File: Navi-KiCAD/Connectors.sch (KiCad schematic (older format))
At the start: 7 parts, among them J4 473460001, J5 AXK5S80047YG, J6 AXK5S80047YG, U13 NUF2042XV6T1G

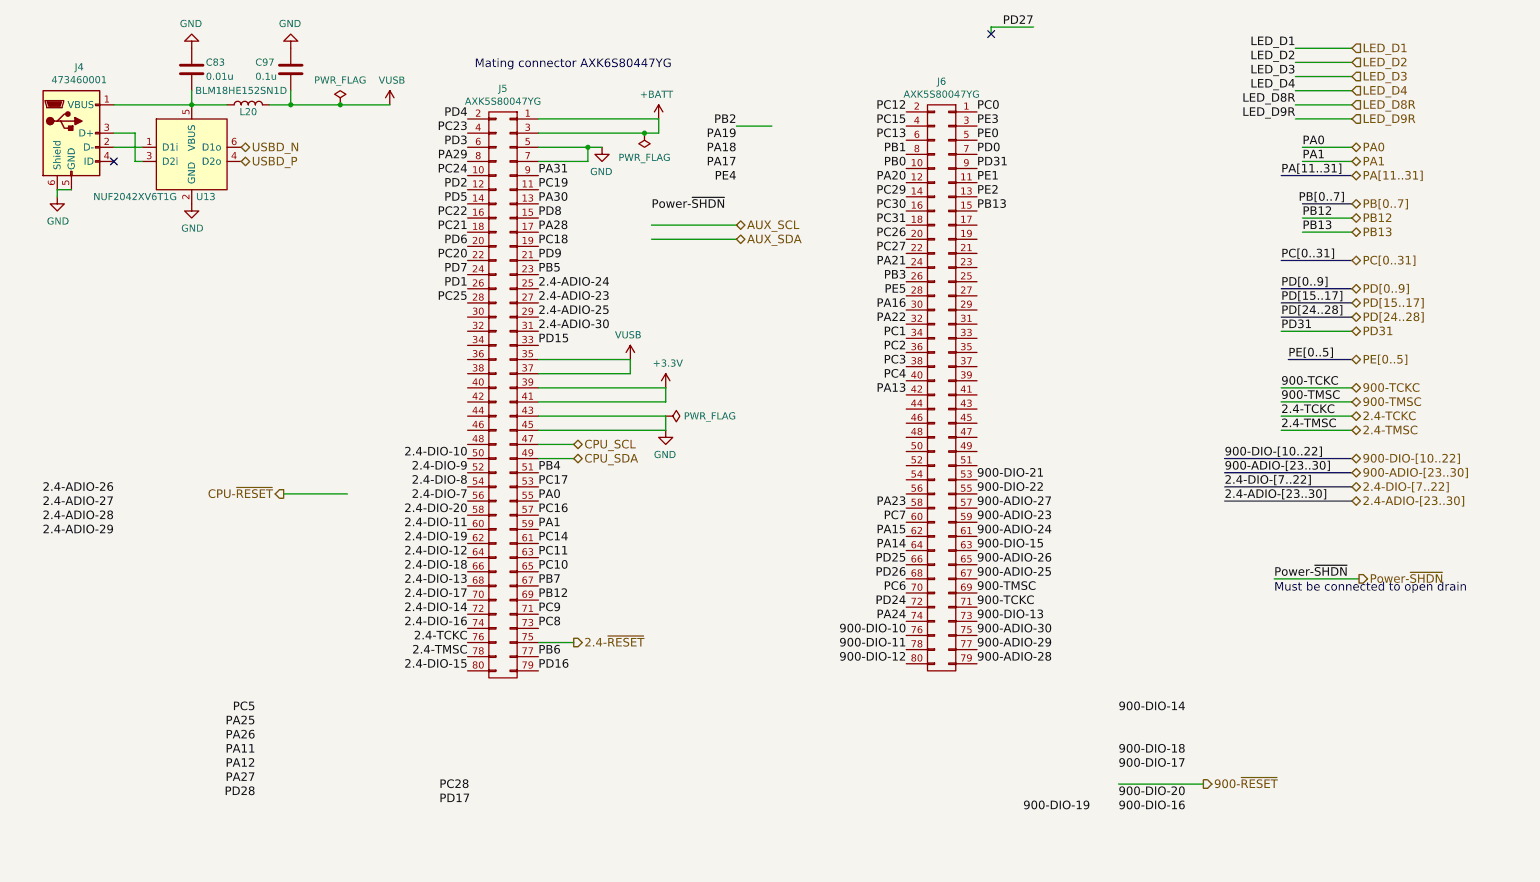
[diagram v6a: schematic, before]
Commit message: Finished reroute
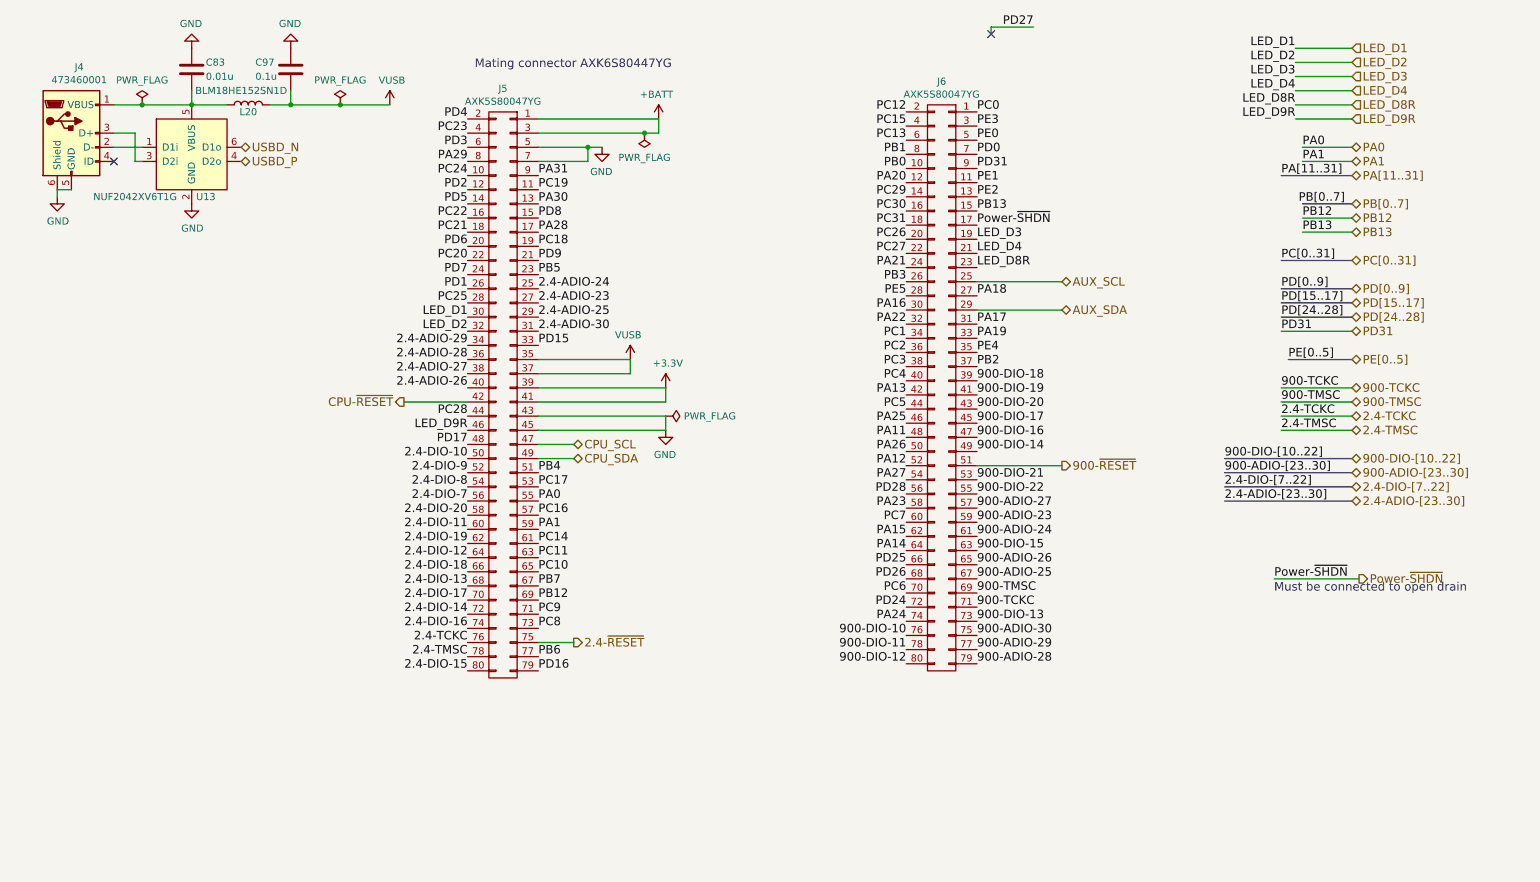
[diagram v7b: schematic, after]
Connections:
- wire segments 52 -> 51
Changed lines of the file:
@@
 Text HLabel 2150 1600 2    60   BiDi ~ 0
 USBD_N
-Text HLabel 2450 4050 0    60   Output ~ 0
+Text HLabel 3300 3400 0    60   Output ~ 0
 CPU-~RESET
-Text HLabel 8950 6100 2    60   Output ~ 0
+Text HLabel 7950 3850 2    60   Output ~ 0
 900-~RESET
 Text HLabel 4500 5100 2    60   Output ~ 0
@@
 Text HLabel 10000 2900 2    60   BiDi ~ 0
 PD31
-Text HLabel 5650 2250 2    60   BiDi ~ 0
+Text HLabel 7950 2750 2    60   BiDi ~ 0
 AUX_SDA
-Text HLabel 5650 2150 2    60   BiDi ~ 0
+Text HLabel 7950 2550 2    60   BiDi ~ 0
 AUX_SCL
 Text HLabel 4500 3800 2    60   BiDi ~ 0
@@
 Text Label 4250 2800 0    60   ~ 0
 2.4-ADIO-25
-Text Label 1250 4050 2    60   ~ 0
+Text Label 3750 3300 2    60   ~ 0
 2.4-ADIO-26
-Text Label 1250 4150 2    60   ~ 0
+Text Label 3750 3200 2    60   ~ 0
 2.4-ADIO-27
-Text Label 1250 4250 2    60   ~ 0
+Text Label 3750 3100 2    60   ~ 0
 2.4-ADIO-28
-Text Label 1250 4350 2    60   ~ 0
+Text Label 3750 3000 2    60   ~ 0
 2.4-ADIO-29
 Text Label 4250 2900 0    60   ~ 0
 2.4-ADIO-30
-Text Label 3550 6250 0    60   ~ 0
+Text Label 3750 3700 2    60   ~ 0
 PD17
-Text Label 3550 6150 0    60   ~ 0
+Text Label 3750 3500 2    60   ~ 0
 PC28
 Wire Wire Line
@@
 Text Label 6850 1850 2    60   ~ 0
 PA20
-Text Label 5650 1550 2    60   ~ 0
+Text Label 7350 2950 0    60   ~ 0
 PA19
-Text Label 5650 1650 2    60   ~ 0
+Text Label 7350 2650 0    60   ~ 0
 PA18
-Text Label 5650 1750 2    60   ~ 0
+Text Label 7350 2850 0    60   ~ 0
 PA17
-Text Label 5650 1450 2    60   ~ 0
+Text Label 7350 3150 0    60   ~ 0
 PB2
-Text Label 5650 1850 2    60   ~ 0
+Text Label 7350 3050 0    60   ~ 0
 PE4
 Text Label 6850 2650 2    60   ~ 0
@@
 Text Label 6850 2450 2    60   ~ 0
 PA21
-Text Label 8350 6300 0    60   ~ 0
+Text Label 7350 3650 0    60   ~ 0
 900-DIO-16
-Text Label 8350 6200 0    60   ~ 0
+Text Label 7350 3450 0    60   ~ 0
 900-DIO-20
 Wire Wire Line
-	8350 6100 8950 6100
+	7350 3850 7950 3850
 Text Label 7350 3950 0    60   ~ 0
 900-DIO-21
-Text Label 8350 6000 0    60   ~ 0
+Text Label 7350 3550 0    60   ~ 0
 900-DIO-17
-Text Label 8350 5900 0    60   ~ 0
+Text Label 7350 3250 0    60   ~ 0
 900-DIO-18
 Text Label 7350 4050 0    60   ~ 0
 900-DIO-22
-Text Label 8150 6300 2    60   ~ 0
+Text Label 7350 3350 0    60   ~ 0
 900-DIO-19
 Text Label 3750 2700 2    60   ~ 0
@@
 Text Label 7350 4950 0    60   ~ 0
 900-DIO-13
-Text Label 8350 5600 0    60   ~ 0
+Text Label 7350 3750 0    60   ~ 0
 900-DIO-14
 Text Label 7350 4450 0    60   ~ 0
 900-DIO-15
 Wire Wire Line
-	5650 2150 5050 2150
-Wire Wire Line
-	5650 2250 5050 2250
-Wire Wire Line
-	2900 4050 2450 4050
-Text Label 2250 6200 2    60   ~ 0
+	7950 2550 7350 2550
+Wire Wire Line
+	7950 2750 7350 2750
+Wire Wire Line
+	3750 3400 3300 3400
+Text Label 6850 4050 2    60   ~ 0
 PD28
-Text Label 2250 6100 2    60   ~ 0
+Text Label 6850 3950 2    60   ~ 0
 PA27
-Text Label 2250 6000 2    60   ~ 0
+Text Label 6850 3850 2    60   ~ 0
 PA12
-Text Label 2250 5900 2    60   ~ 0
+Text Label 6850 3650 2    60   ~ 0
 PA11
-Text Label 2250 5800 2    60   ~ 0
+Text Label 6850 3750 2    60   ~ 0
 PA26
-Text Label 2250 5700 2    60   ~ 0
+Text Label 6850 3550 2    60   ~ 0
 PA25
-Text Label 2250 5600 2    60   ~ 0
+Text Label 6850 3450 2    60   ~ 0
 PC5
 Text Label 6850 4950 2    60   ~ 0
@@
 Text Label 4250 4800 0    60   ~ 0
 PB12
-Text Label 5050 2050 0    60   ~ 0
+Text Label 7350 2150 0    60   ~ 0
 Power-~SHDN
 Wire Wire Line
@@
 	2500 1300 2500 1200
 Connection ~ 2500 1300
-Wire Wire Line
-	5650 1450 5900 1450
 Wire Wire Line
 	4250 5100 4500 5100
@@
 	7450 750  7450 800
 NoConn ~ 7450 800
+Text Label 3750 2800 2    60   ~ 0
+LED_D1
+Text Label 3750 2900 2    60   ~ 0
+LED_D2
+Text Label 7350 2250 0    60   ~ 0
+LED_D3
+Text Label 7350 2350 0    60   ~ 0
+LED_D4
+Text Label 7350 2450 0    60   ~ 0
+LED_D8R
+Text Label 3750 3600 2    60   ~ 0
+LED_D9R
+$Comp
+L PWR_FLAG #FLG0145
+U 1 1 59007451
+P 1450 1300
+F 0 "#FLG0145" H -4200 -125 50  0001 C CNN
+F 1 "PWR_FLAG" H 1450 1474 50  0000 C CNN
+F 2 "" H -4200 -200 50  0001 C CNN
+F 3 "" H -4200 -200 50  0001 C CNN
+	1    1450 1300
+	1    0    0    -1
+$EndComp
+Connection ~ 1450 1300
 $EndSCHEMATC

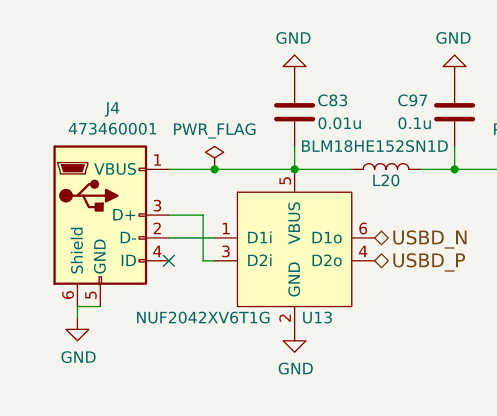
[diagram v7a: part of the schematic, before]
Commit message: Cleaned up 3D models and rebuilt outputs.
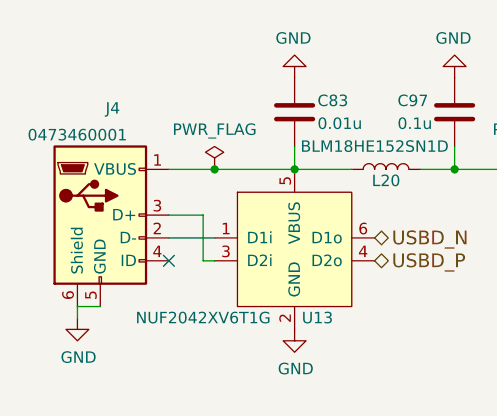
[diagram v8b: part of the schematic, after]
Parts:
- J4: value 473460001 -> 0473460001
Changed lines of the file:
@@
 P 950 1500
 F 0 "J4" H 1005 1967 50  0000 C CNN
-F 1 "473460001" H 1005 1876 50  0000 C CNN
+F 1 "0473460001" H 850 1850 50  0000 C CNN
 F 2 "Connectors:USB_Micro-B_0473460001" H -3700 -1300 50  0001 C CNN
 F 3 "http://www.molex.com/pdm_docs/sd/473460001_sd.pdf" H -3700 -1300 50  0001 C CNN
